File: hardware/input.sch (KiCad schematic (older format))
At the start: 65 parts, among them Q1 Si2302CDS, Q10 Si2302CDS, Q2 Si2302CDS, Q3 Si2302CDS, Q4 Si2302CDS, Q5 Si2302CDS, Q6 Si2302CDS, Q7 Si2302CDS, Q8 Si2302CDS, Q9 Si2302CDS

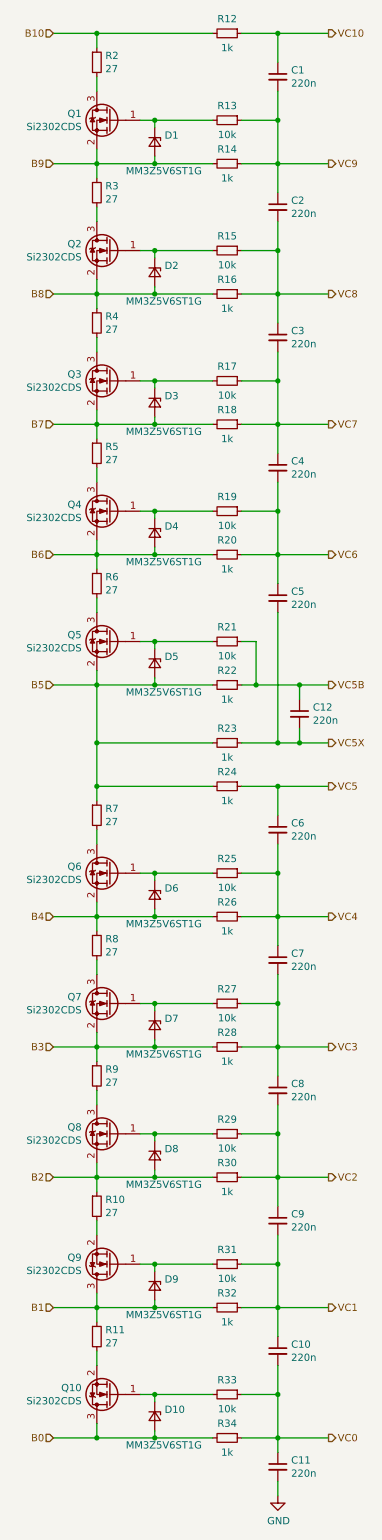
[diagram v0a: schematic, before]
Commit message: finish clean-up and part assignment
Signed-off-by: Ene Alexandru <ene.alexandru@gmail.com>
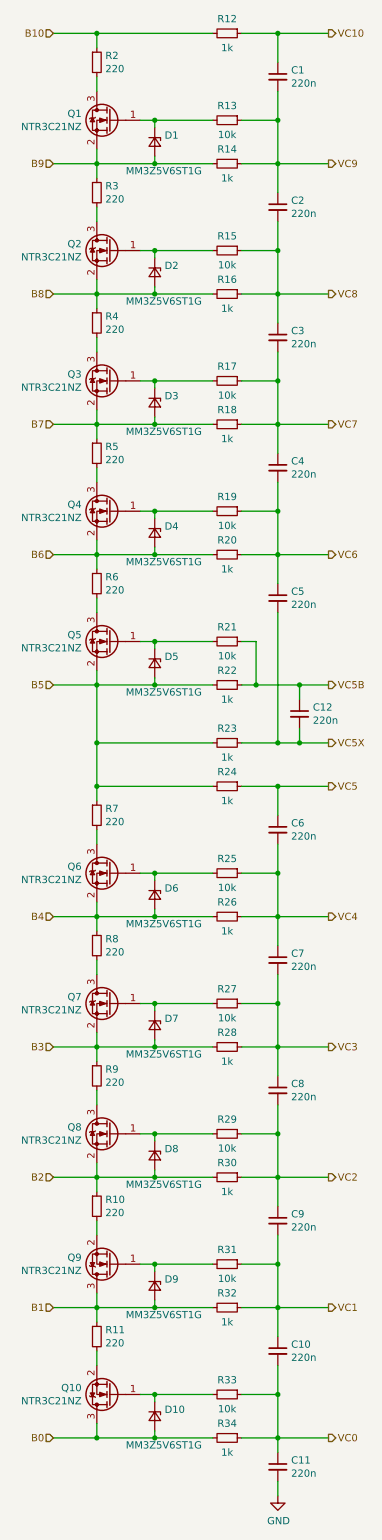
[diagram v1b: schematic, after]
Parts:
- Q1, Q10, Q2, Q3, Q4, Q5, Q6, Q7, Q8, Q9: value Si2302CDS -> NTR3C21NZ
- R10, R11, R2, R3, R4, R5, R6, R7, R8, R9: value 27 -> 220
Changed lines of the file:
@@
 P 3400 1200
 F 0 "R2" H 3459 1246 50  0000 L CNN
-F 1 "27" H 3459 1155 50  0000 L CNN
+F 1 "220" H 3459 1155 50  0000 L CNN
 F 2 "Resistor_SMD:R_1206_3216Metric_Pad1.42x1.75mm_HandSolder" H 3400 1200 50  0001 C CNN
 F 3 "~" H 3400 1200 50  0001 C CNN
@@
 P 3400 2100
 F 0 "R3" H 3459 2146 50  0000 L CNN
-F 1 "27" H 3459 2055 50  0000 L CNN
+F 1 "220" H 3459 2055 50  0000 L CNN
 F 2 "Resistor_SMD:R_1206_3216Metric_Pad1.42x1.75mm_HandSolder" H 3400 2100 50  0001 C CNN
 F 3 "~" H 3400 2100 50  0001 C CNN
@@
 P 3400 3000
 F 0 "R4" H 3459 3046 50  0000 L CNN
-F 1 "27" H 3459 2955 50  0000 L CNN
+F 1 "220" H 3459 2955 50  0000 L CNN
 F 2 "Resistor_SMD:R_1206_3216Metric_Pad1.42x1.75mm_HandSolder" H 3400 3000 50  0001 C CNN
 F 3 "~" H 3400 3000 50  0001 C CNN
@@
 P 3400 3900
 F 0 "R5" H 3459 3946 50  0000 L CNN
-F 1 "27" H 3459 3855 50  0000 L CNN
+F 1 "220" H 3459 3855 50  0000 L CNN
 F 2 "Resistor_SMD:R_1206_3216Metric_Pad1.42x1.75mm_HandSolder" H 3400 3900 50  0001 C CNN
 F 3 "~" H 3400 3900 50  0001 C CNN
@@
 P 3400 4800
 F 0 "R6" H 3459 4846 50  0000 L CNN
-F 1 "27" H 3459 4755 50  0000 L CNN
+F 1 "220" H 3459 4755 50  0000 L CNN
 F 2 "Resistor_SMD:R_1206_3216Metric_Pad1.42x1.75mm_HandSolder" H 3400 4800 50  0001 C CNN
 F 3 "~" H 3400 4800 50  0001 C CNN
@@
 P 3400 6400
 F 0 "R7" H 3459 6446 50  0000 L CNN
-F 1 "27" H 3459 6355 50  0000 L CNN
+F 1 "220" H 3459 6355 50  0000 L CNN
 F 2 "Resistor_SMD:R_1206_3216Metric_Pad1.42x1.75mm_HandSolder" H 3400 6400 50  0001 C CNN
 F 3 "~" H 3400 6400 50  0001 C CNN
@@
 P 3400 7300
 F 0 "R8" H 3459 7346 50  0000 L CNN
-F 1 "27" H 3459 7255 50  0000 L CNN
+F 1 "220" H 3459 7255 50  0000 L CNN
 F 2 "Resistor_SMD:R_1206_3216Metric_Pad1.42x1.75mm_HandSolder" H 3400 7300 50  0001 C CNN
 F 3 "~" H 3400 7300 50  0001 C CNN
@@
 P 3400 8200
 F 0 "R9" H 3459 8246 50  0000 L CNN
-F 1 "27" H 3459 8155 50  0000 L CNN
+F 1 "220" H 3459 8155 50  0000 L CNN
 F 2 "Resistor_SMD:R_1206_3216Metric_Pad1.42x1.75mm_HandSolder" H 3400 8200 50  0001 C CNN
 F 3 "~" H 3400 8200 50  0001 C CNN
@@
 P 3400 9100
 F 0 "R10" H 3459 9146 50  0000 L CNN
-F 1 "27" H 3459 9055 50  0000 L CNN
+F 1 "220" H 3459 9055 50  0000 L CNN
 F 2 "Resistor_SMD:R_1206_3216Metric_Pad1.42x1.75mm_HandSolder" H 3400 9100 50  0001 C CNN
 F 3 "~" H 3400 9100 50  0001 C CNN
@@
 P 3400 10000
 F 0 "R11" H 3459 10046 50  0000 L CNN
-F 1 "27" H 3459 9955 50  0000 L CNN
+F 1 "220" H 3459 9955 50  0000 L CNN
 F 2 "Resistor_SMD:R_1206_3216Metric_Pad1.42x1.75mm_HandSolder" H 3400 10000 50  0001 C CNN
 F 3 "~" H 3400 10000 50  0001 C CNN
@@
 P 3500 1600
 F 0 "Q1" H 3705 1646 50  0000 L CNN
-F 1 "Si2302CDS" H 3705 1555 50  0000 L CNN
+F 1 "NTR3C21NZ" H 3705 1555 50  0000 L CNN
 F 2 "Package_TO_SOT_SMD:SOT-23" H 3700 1700 50  0001 C CNN
 F 3 "~" H 3500 1600 50  0001 C CNN
@@
 P 3500 2500
 F 0 "Q2" H 3705 2546 50  0000 L CNN
-F 1 "Si2302CDS" H 3705 2455 50  0000 L CNN
+F 1 "NTR3C21NZ" H 3705 2455 50  0000 L CNN
 F 2 "Package_TO_SOT_SMD:SOT-23" H 3700 2600 50  0001 C CNN
 F 3 "~" H 3500 2500 50  0001 C CNN
@@
 P 3500 3400
 F 0 "Q3" H 3705 3446 50  0000 L CNN
-F 1 "Si2302CDS" H 3705 3355 50  0000 L CNN
+F 1 "NTR3C21NZ" H 3705 3355 50  0000 L CNN
 F 2 "Package_TO_SOT_SMD:SOT-23" H 3700 3500 50  0001 C CNN
 F 3 "~" H 3500 3400 50  0001 C CNN
@@
 P 3500 4300
 F 0 "Q4" H 3705 4346 50  0000 L CNN
-F 1 "Si2302CDS" H 3705 4255 50  0000 L CNN
+F 1 "NTR3C21NZ" H 3705 4255 50  0000 L CNN
 F 2 "Package_TO_SOT_SMD:SOT-23" H 3700 4400 50  0001 C CNN
 F 3 "~" H 3500 4300 50  0001 C CNN
@@
 P 3500 5200
 F 0 "Q5" H 3705 5246 50  0000 L CNN
-F 1 "Si2302CDS" H 3705 5155 50  0000 L CNN
+F 1 "NTR3C21NZ" H 3705 5155 50  0000 L CNN
 F 2 "Package_TO_SOT_SMD:SOT-23" H 3700 5300 50  0001 C CNN
 F 3 "~" H 3500 5200 50  0001 C CNN
@@
 P 3500 6800
 F 0 "Q6" H 3705 6846 50  0000 L CNN
-F 1 "Si2302CDS" H 3705 6755 50  0000 L CNN
+F 1 "NTR3C21NZ" H 3705 6755 50  0000 L CNN
 F 2 "Package_TO_SOT_SMD:SOT-23" H 3700 6900 50  0001 C CNN
 F 3 "~" H 3500 6800 50  0001 C CNN
@@
 P 3500 7700
 F 0 "Q7" H 3705 7746 50  0000 L CNN
-F 1 "Si2302CDS" H 3705 7655 50  0000 L CNN
+F 1 "NTR3C21NZ" H 3705 7655 50  0000 L CNN
 F 2 "Package_TO_SOT_SMD:SOT-23" H 3700 7800 50  0001 C CNN
 F 3 "~" H 3500 7700 50  0001 C CNN
@@
 P 3500 8600
 F 0 "Q8" H 3705 8646 50  0000 L CNN
-F 1 "Si2302CDS" H 3705 8555 50  0000 L CNN
+F 1 "NTR3C21NZ" H 3705 8555 50  0000 L CNN
 F 2 "Package_TO_SOT_SMD:SOT-23" H 3700 8700 50  0001 C CNN
 F 3 "~" H 3500 8600 50  0001 C CNN
@@
 P 3500 9500
 F 0 "Q9" H 3705 9454 50  0000 L CNN
-F 1 "Si2302CDS" H 3705 9545 50  0000 L CNN
+F 1 "NTR3C21NZ" H 3705 9545 50  0000 L CNN
 F 2 "Package_TO_SOT_SMD:SOT-23" H 3700 9600 50  0001 C CNN
 F 3 "~" H 3500 9500 50  0001 C CNN
@@
 P 3500 10400
 F 0 "Q10" H 3705 10354 50  0000 L CNN
-F 1 "Si2302CDS" H 3705 10445 50  0000 L CNN
+F 1 "NTR3C21NZ" H 3705 10445 50  0000 L CNN
 F 2 "Package_TO_SOT_SMD:SOT-23" H 3700 10500 50  0001 C CNN
 F 3 "~" H 3500 10400 50  0001 C CNN

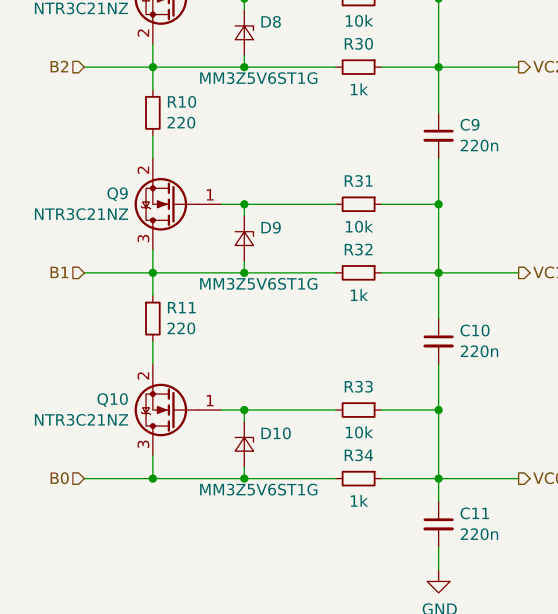
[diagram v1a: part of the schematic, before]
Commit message: almost ready for pcb, needs revision
Signed-off-by: Ene Alexandru <ene.alexandru@gmail.com>
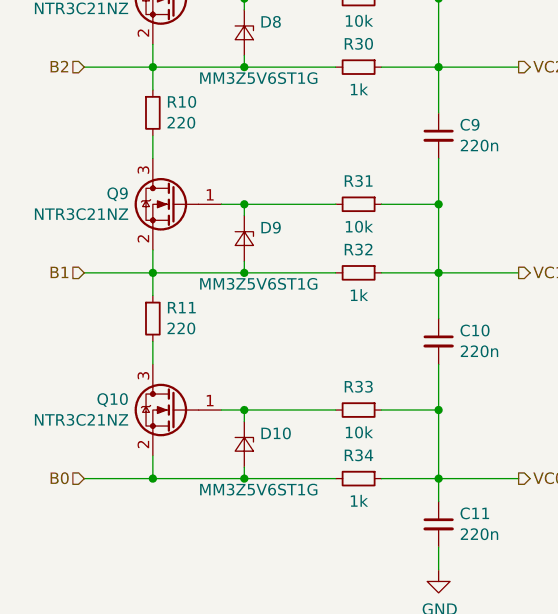
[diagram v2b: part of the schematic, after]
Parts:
- R10, R11, R2, R3, R4, R5, R6, R7, R8, R9: footprint Resistor_SMD:R_1206_3216Metric_Pad1.42x1.75mm_HandSolder -> Resistor_SMD:R_0805_2012Metric_Pad1.15x1.40mm_HandSolder
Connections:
- net B0: now also Q10.2 (S); no longer Q10.3 (D)
- net B1: now also Q9.2 (S); no longer Q9.3 (D)
- net at R10.2: now also Q9.3 (D); no longer Q9.2 (S)
- net at R11.2: now also Q10.3 (D); no longer Q10.2 (S)
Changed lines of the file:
@@
 F 0 "R2" H 3459 1246 50  0000 L CNN
 F 1 "220" H 3459 1155 50  0000 L CNN
-F 2 "Resistor_SMD:R_1206_3216Metric_Pad1.42x1.75mm_HandSolder" H 3400 1200 50  0001 C CNN
+F 2 "Resistor_SMD:R_0805_2012Metric_Pad1.15x1.40mm_HandSolder" H 3400 1200 50  0001 C CNN
 F 3 "~" H 3400 1200 50  0001 C CNN
 	1    3400 1200
@@
 F 0 "R3" H 3459 2146 50  0000 L CNN
 F 1 "220" H 3459 2055 50  0000 L CNN
-F 2 "Resistor_SMD:R_1206_3216Metric_Pad1.42x1.75mm_HandSolder" H 3400 2100 50  0001 C CNN
+F 2 "Resistor_SMD:R_0805_2012Metric_Pad1.15x1.40mm_HandSolder" H 3400 2100 50  0001 C CNN
 F 3 "~" H 3400 2100 50  0001 C CNN
 	1    3400 2100
@@
 F 0 "R4" H 3459 3046 50  0000 L CNN
 F 1 "220" H 3459 2955 50  0000 L CNN
-F 2 "Resistor_SMD:R_1206_3216Metric_Pad1.42x1.75mm_HandSolder" H 3400 3000 50  0001 C CNN
+F 2 "Resistor_SMD:R_0805_2012Metric_Pad1.15x1.40mm_HandSolder" H 3400 3000 50  0001 C CNN
 F 3 "~" H 3400 3000 50  0001 C CNN
 	1    3400 3000
@@
 F 0 "R5" H 3459 3946 50  0000 L CNN
 F 1 "220" H 3459 3855 50  0000 L CNN
-F 2 "Resistor_SMD:R_1206_3216Metric_Pad1.42x1.75mm_HandSolder" H 3400 3900 50  0001 C CNN
+F 2 "Resistor_SMD:R_0805_2012Metric_Pad1.15x1.40mm_HandSolder" H 3400 3900 50  0001 C CNN
 F 3 "~" H 3400 3900 50  0001 C CNN
 	1    3400 3900
@@
 F 0 "R6" H 3459 4846 50  0000 L CNN
 F 1 "220" H 3459 4755 50  0000 L CNN
-F 2 "Resistor_SMD:R_1206_3216Metric_Pad1.42x1.75mm_HandSolder" H 3400 4800 50  0001 C CNN
+F 2 "Resistor_SMD:R_0805_2012Metric_Pad1.15x1.40mm_HandSolder" H 3400 4800 50  0001 C CNN
 F 3 "~" H 3400 4800 50  0001 C CNN
 	1    3400 4800
@@
 F 0 "R7" H 3459 6446 50  0000 L CNN
 F 1 "220" H 3459 6355 50  0000 L CNN
-F 2 "Resistor_SMD:R_1206_3216Metric_Pad1.42x1.75mm_HandSolder" H 3400 6400 50  0001 C CNN
+F 2 "Resistor_SMD:R_0805_2012Metric_Pad1.15x1.40mm_HandSolder" H 3400 6400 50  0001 C CNN
 F 3 "~" H 3400 6400 50  0001 C CNN
 	1    3400 6400
@@
 F 0 "R8" H 3459 7346 50  0000 L CNN
 F 1 "220" H 3459 7255 50  0000 L CNN
-F 2 "Resistor_SMD:R_1206_3216Metric_Pad1.42x1.75mm_HandSolder" H 3400 7300 50  0001 C CNN
+F 2 "Resistor_SMD:R_0805_2012Metric_Pad1.15x1.40mm_HandSolder" H 3400 7300 50  0001 C CNN
 F 3 "~" H 3400 7300 50  0001 C CNN
 	1    3400 7300
@@
 F 0 "R9" H 3459 8246 50  0000 L CNN
 F 1 "220" H 3459 8155 50  0000 L CNN
-F 2 "Resistor_SMD:R_1206_3216Metric_Pad1.42x1.75mm_HandSolder" H 3400 8200 50  0001 C CNN
+F 2 "Resistor_SMD:R_0805_2012Metric_Pad1.15x1.40mm_HandSolder" H 3400 8200 50  0001 C CNN
 F 3 "~" H 3400 8200 50  0001 C CNN
 	1    3400 8200
@@
 F 0 "R10" H 3459 9146 50  0000 L CNN
 F 1 "220" H 3459 9055 50  0000 L CNN
-F 2 "Resistor_SMD:R_1206_3216Metric_Pad1.42x1.75mm_HandSolder" H 3400 9100 50  0001 C CNN
+F 2 "Resistor_SMD:R_0805_2012Metric_Pad1.15x1.40mm_HandSolder" H 3400 9100 50  0001 C CNN
 F 3 "~" H 3400 9100 50  0001 C CNN
 	1    3400 9100
@@
 F 0 "R11" H 3459 10046 50  0000 L CNN
 F 1 "220" H 3459 9955 50  0000 L CNN
-F 2 "Resistor_SMD:R_1206_3216Metric_Pad1.42x1.75mm_HandSolder" H 3400 10000 50  0001 C CNN
+F 2 "Resistor_SMD:R_0805_2012Metric_Pad1.15x1.40mm_HandSolder" H 3400 10000 50  0001 C CNN
 F 3 "~" H 3400 10000 50  0001 C CNN
 	1    3400 10000
@@
 $Comp
 L Device:Q_NMOS_GSD Q9
-U 1 1 5E2085D2
+U 1 1 5E32B60E
 P 3500 9500
-F 0 "Q9" H 3705 9454 50  0000 L CNN
-F 1 "NTR3C21NZ" H 3705 9545 50  0000 L CNN
+F 0 "Q9" H 3705 9546 50  0000 L CNN
+F 1 "NTR3C21NZ" H 3705 9455 50  0000 L CNN
 F 2 "Package_TO_SOT_SMD:SOT-23" H 3700 9600 50  0001 C CNN
 F 3 "~" H 3500 9500 50  0001 C CNN
 	1    3500 9500
-	-1   0    0    1
+	-1   0    0    -1
 $EndComp
 $Comp
 L Device:Q_NMOS_GSD Q10
-U 1 1 5E210FCC
+U 1 1 5E32C76C
 P 3500 10400
-F 0 "Q10" H 3705 10354 50  0000 L CNN
-F 1 "NTR3C21NZ" H 3705 10445 50  0000 L CNN
+F 0 "Q10" H 3705 10446 50  0000 L CNN
+F 1 "NTR3C21NZ" H 3705 10355 50  0000 L CNN
 F 2 "Package_TO_SOT_SMD:SOT-23" H 3700 10500 50  0001 C CNN
 F 3 "~" H 3500 10400 50  0001 C CNN
 	1    3500 10400
-	-1   0    0    1
+	-1   0    0    -1
 $EndComp
 $EndSCHEMATC
